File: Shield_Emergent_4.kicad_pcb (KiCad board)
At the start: 4 copper layers, 27 x 36 mm, 37 parts, among them J1 TF31-18S-0.5SH_800_, J2 Conn_01x04_Socket, J3 TF31-18S-0.5SH_800_, J4 Conn_01x05, J5 Conn_01x02_Socket, J6 Conn_01x02_Socket, J7 Conn_01x05, J8 Conn_02x05_Odd_Even, U3 SP3012-06UTG, U4 SP3012-06UTG, U5 SP3012-06UTG, U6 SP3012-06UTG, X1 USB_C_24pins

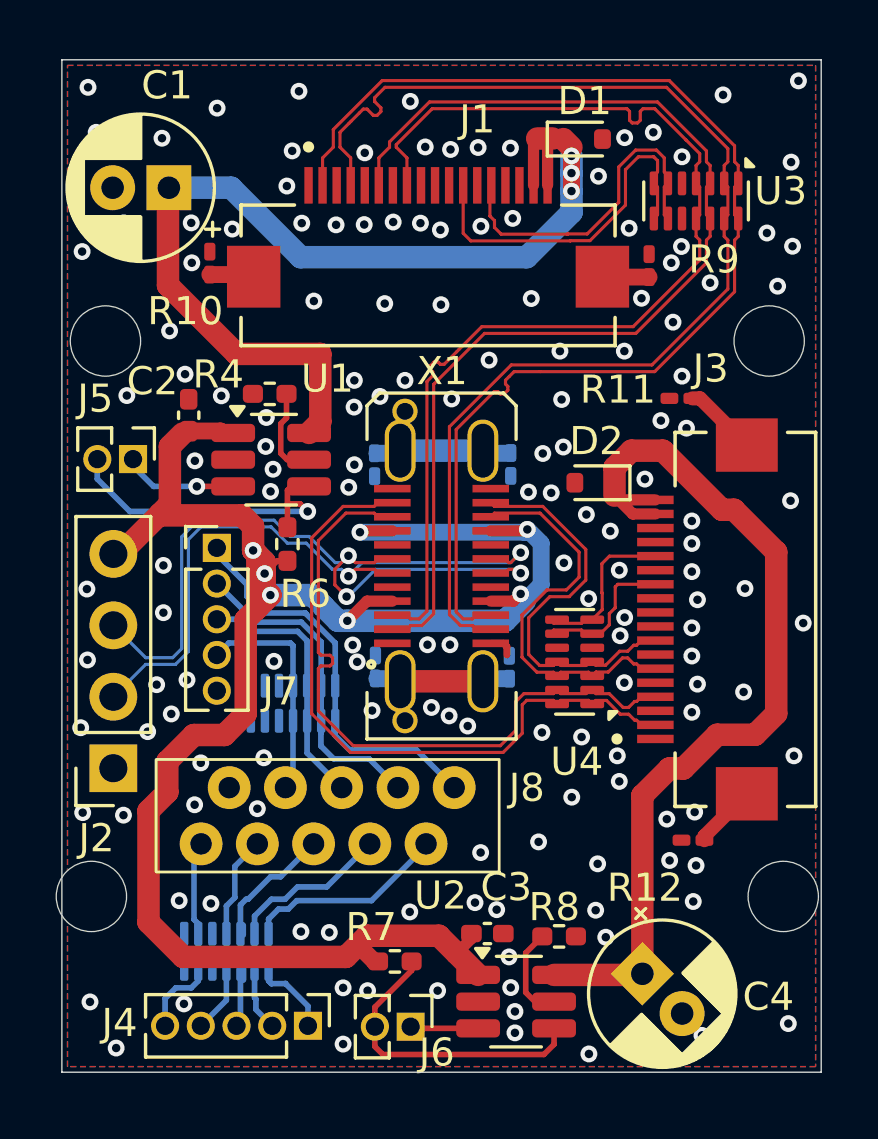
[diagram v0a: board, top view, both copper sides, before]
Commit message: v0.2 draft routing
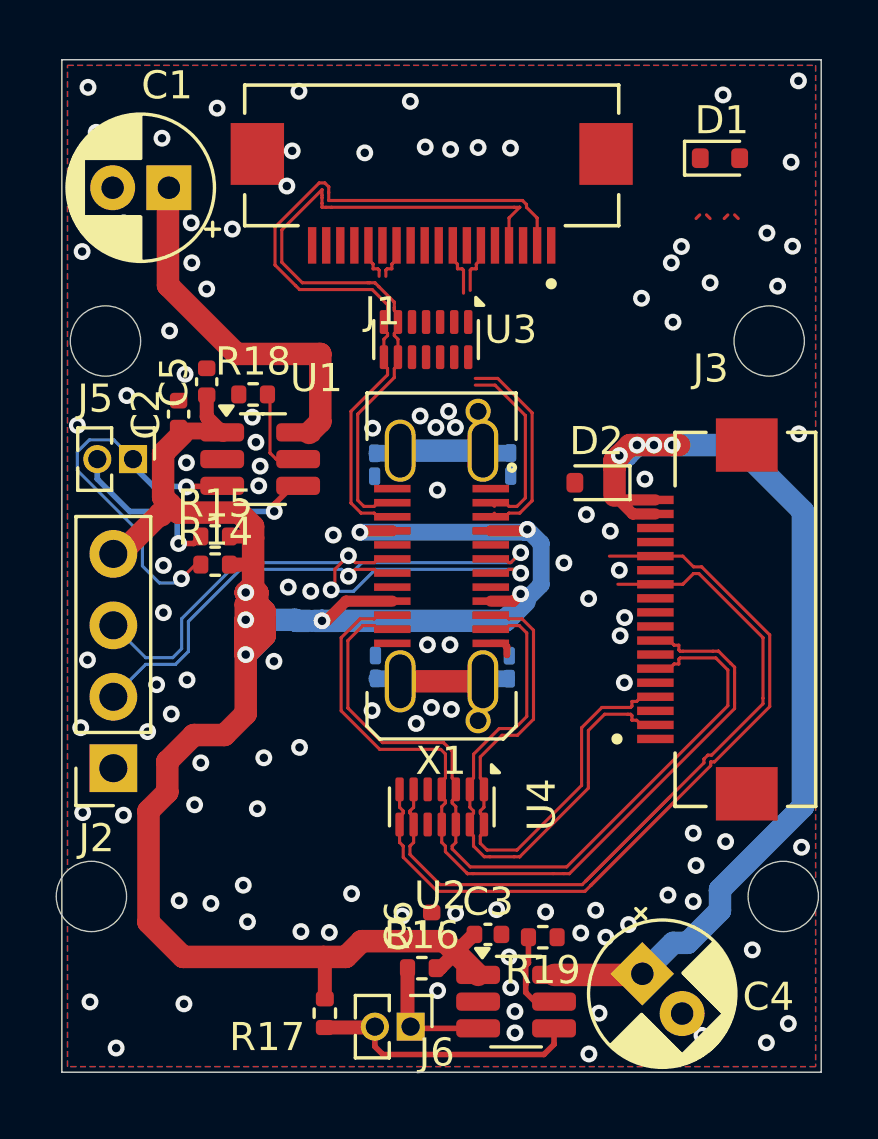
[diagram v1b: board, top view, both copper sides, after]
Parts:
- removed J4, J7: Conn_01x05, Connector_PinHeader_1.27mm:PinHeader_1x05_P1.27mm_Vertical
- removed J8: Conn_02x05_Odd_Even, myLib8:DS1020-04-10BVT1
- removed R10, R11, R12, R9: 0, Resistor_SMD:R_0201_0603Metric_Pad0.64x0.40mm_HandSolder
- removed R4, R8: R, Resistor_SMD:R_0402_1005Metric_Pad0.72x0.64mm_HandSolder
- removed R6, R7: 100k, Resistor_SMD:R_0402_1005Metric_Pad0.72x0.64mm_HandSolder
- removed U5, U6: SP3012-06UTG, myLib8:DFN-14_1.35x3.5mm_P0.5mm
- added C5: 10 u, Capacitor_SMD:C_0402_1005Metric, F.Cu at (5.15, 11.4)
- added C6: 10 u, Capacitor_SMD:C_0402_1005Metric, F.Cu at (13.2, 30.8)
- added R14: 100k, Resistor_SMD:R_0402_1005Metric, F.Cu at (5.45, 17.9)
- added R15: 100k, Resistor_SMD:R_0402_1005Metric, F.Cu at (5.45, 16.9)
- added R16: 100k, Resistor_SMD:R_0402_1005Metric, F.Cu at (12.8, 32.3)
- added R17: 100k, Resistor_SMD:R_0402_1005Metric, F.Cu at (9.35, 33.9)
- added R18: 18 k, Resistor_SMD:R_0402_1005Metric, F.Cu at (6.80, 11.9)
- added R19: 18 k, Resistor_SMD:R_0402_1005Metric, F.Cu at (17.1, 31.2)
- C2, C3: footprint Capacitor_SMD:C_0402_1005Metric_Pad0.74x0.62mm_HandSolder -> Capacitor_SMD:C_0402_1005Metric
- moved U3 10.8 mm to (12.9, 9.95)
- moved U4 7.00 mm to (13.5, 26.6), turned to -90 degrees
- moved D1 4.92 mm to (23.4, 3.50)
- moved J1 4.27 mm to (13.2, 3.40), turned to 0 degrees
- moved U1 0.39 mm to (7.05, 14.2)
- moved C2 0.36 mm to (4.15, 12.6)
- turned X1 to -90 degrees
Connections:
- J1 pad 12: 1_D+ -> 1_D-
- J1 pad 14: 1_D- -> 1_D+
- J1 pad 6: TX1+ -> TX1-
- J1 pad 8: TX1- -> TX1+
- J1 pad S1: Net-(J1-PadS1) -> GND
- J1 pad S2: Net-(J1-PadS2) -> GND
- J3 pad 2: RX2+ -> RX2-
- J3 pad 4: RX2- -> RX2+
- J3 pad 6: TX2- -> TX2+
- J3 pad 8: TX2+ -> TX2-
- J3 pad S1: Net-(J3-PadS1) -> GND
- J3 pad S2: Net-(J3-PadS2) -> GND
- U3 pad 1: RX1- -> TX1-
- U3 pad 11: TX1- -> 1_D+
- U3 pad 12: TX1+ -> 1_D-
- U3 pad 13: RX1+ -> TX1+
- U3 pad 14: RX1- -> TX1-
- U3 pad 2: RX1+ -> TX1+
- U3 pad 3: TX1+ -> 1_D-
- U3 pad 4: TX1- -> 1_D+
- U3 pad 6: 1_D- -> RX1+
- U3 pad 7: 1_D+ -> RX1-
- U3 pad 8: 1_D+ -> RX1-
- U3 pad 9: 1_D- -> RX1+
- U4 pad 11: TX2+ -> TX2-
- U4 pad 12: TX2- -> TX2+
- U4 pad 3: TX2- -> TX2+
- U4 pad 4: TX2+ -> TX2-
- X1 pad A10: RX2- -> RX2+
- X1 pad A11: RX2+ -> RX2-
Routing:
- net TX1+: track 39.8 -> 8.89 mm
- net TX1-: track 39.8 -> 10.1 mm
- net 2_D-: track 5.68 -> 32.5 mm
- net 2_D+: track 5.00 -> 31.0 mm
- net VOUT1: track 37.2 -> 12.9 mm, vias 3 -> 0
- net RX1+: track 43.7 -> 26.3 mm
- net TX2-: track 14.3 -> 31.1 mm
- net RX1-: track 43.7 -> 27.4 mm
- net TX2+: track 14.3 -> 29.5 mm
- net K2: track 14.6 -> 0.00 mm
- net VBUS: track 71.9 -> 85.3 mm
- net K4: track 11.9 -> 0.00 mm
- net K1: track 11.5 -> 0.00 mm
- net 1_D+: track 13.0 -> 1.86 mm
- net EN1: track 4.10 -> 14.2 mm, vias 1 -> 2
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
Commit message: v0.3 conceptual routing was added
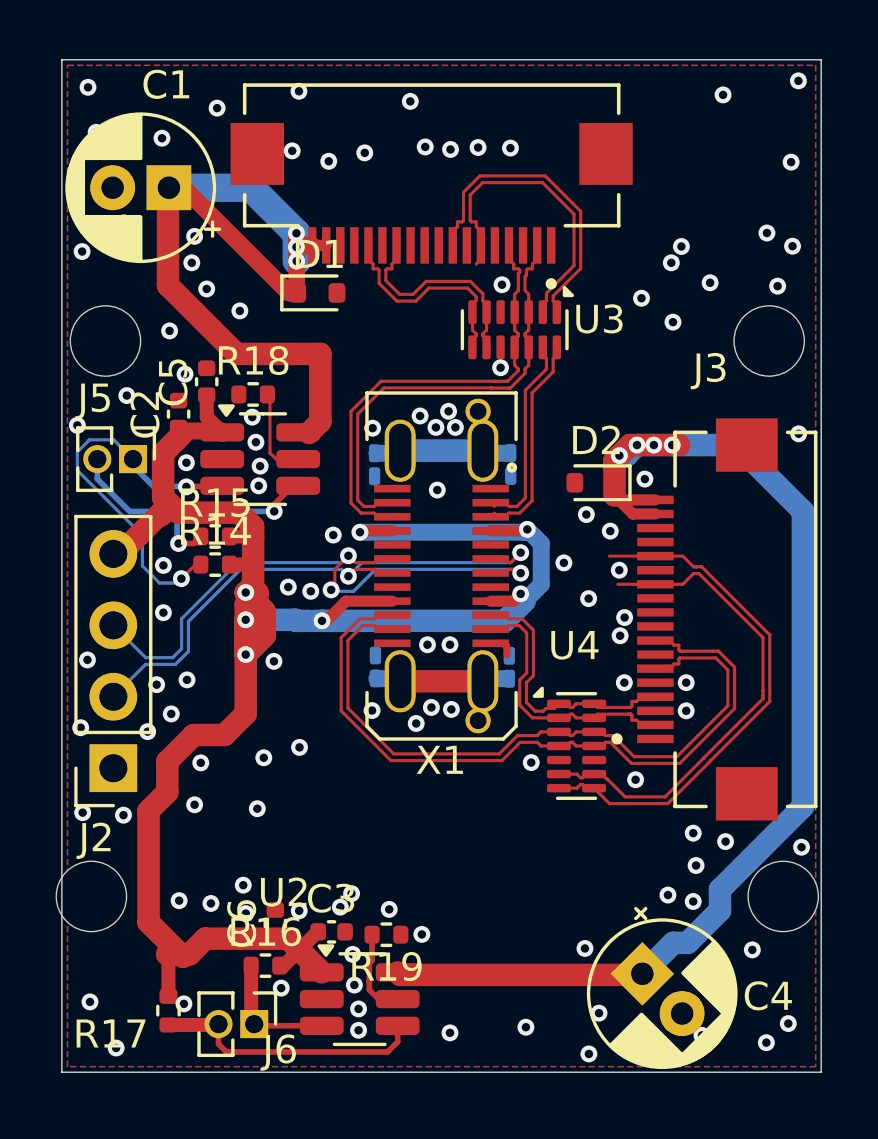
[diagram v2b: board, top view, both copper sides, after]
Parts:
- moved D1 15.1 mm to (9.08, 8.29)
- moved J6 5.56 mm to (6.84, 34.3)
- moved R19 5.56 mm to (11.5, 31.1)
- moved C3 5.56 mm to (9.59, 31.0)
- moved C6 5.56 mm to (7.59, 30.7)
- moved R16 5.56 mm to (7.24, 32.2)
- moved U2 5.56 mm to (10.6, 33.4)
- moved R17 5.56 mm to (3.79, 33.8)
- moved U4 5.26 mm to (18.3, 24.4), turned to 0 degrees
- moved U3 3.17 mm to (16.1, 9.60)
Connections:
- J1 pad 2: RX1- -> RX1+
- J1 pad 4: RX1+ -> RX1-
- J1 pad 6: TX1- -> TX1+
- J1 pad 8: TX1+ -> TX1-
- U3 pad 11: 1_D+ -> RX1-
- U3 pad 12: 1_D- -> RX1+
- U3 pad 3: 1_D- -> RX1+
- U3 pad 4: 1_D+ -> RX1-
- U3 pad 6: RX1+ -> 1_D-
- U3 pad 7: RX1- -> 1_D+
- U3 pad 8: RX1- -> 1_D+
- U3 pad 9: RX1+ -> 1_D-
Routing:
- net VOUT1: track 12.9 -> 28.9 mm, vias 0 -> 3
- net 2_D-: track 32.5 -> 18.6 mm
- net 2_D+: track 31.0 -> 17.6 mm
- net RX1-: track 27.4 -> 16.4 mm
- net RX2+: track 21.0 -> 10.2 mm
- net RX2-: track 21.0 -> 10.2 mm
- net RX1+: track 26.3 -> 16.0 mm
- net TX1+: track 8.89 -> 18.4 mm
- net TX1-: track 10.1 -> 18.8 mm
- net 1_D+: track 1.86 -> 7.60 mm
- net VOUT2: track 36.5 -> 42.1 mm
- net 1_D-: track 2.13 -> 7.60 mm
- net VBUS: track 85.3 -> 80.3 mm
- net TX2-: track 31.1 -> 26.4 mm
- net TX2+: track 29.5 -> 24.8 mm
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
